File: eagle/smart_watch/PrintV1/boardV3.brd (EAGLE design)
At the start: 100 x 80 mm, 62 parts, among them U1 MCP73831, U2 TPS61200, U3 MAX1704X, U4 V_REG_LDOSMD, Y1 16MHz

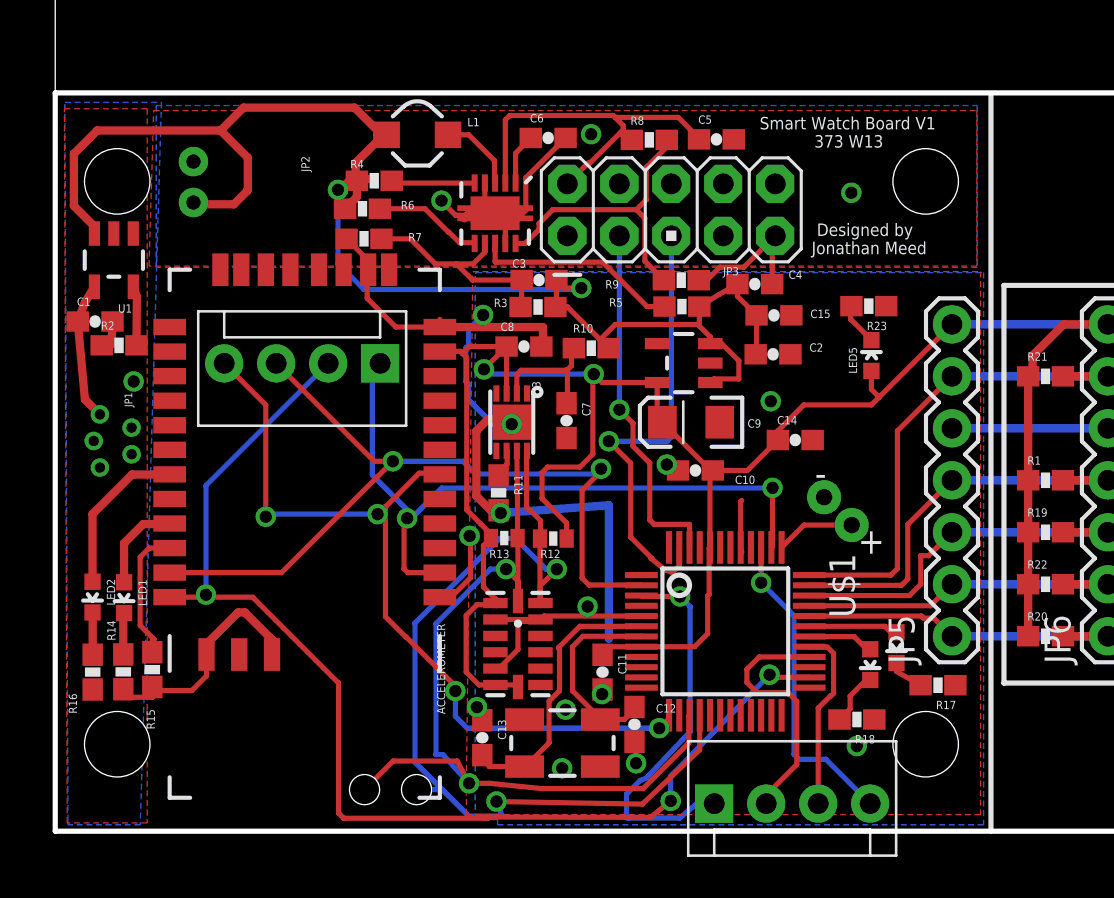
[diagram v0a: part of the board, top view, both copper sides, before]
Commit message: Fixed up git ignore for xpress;
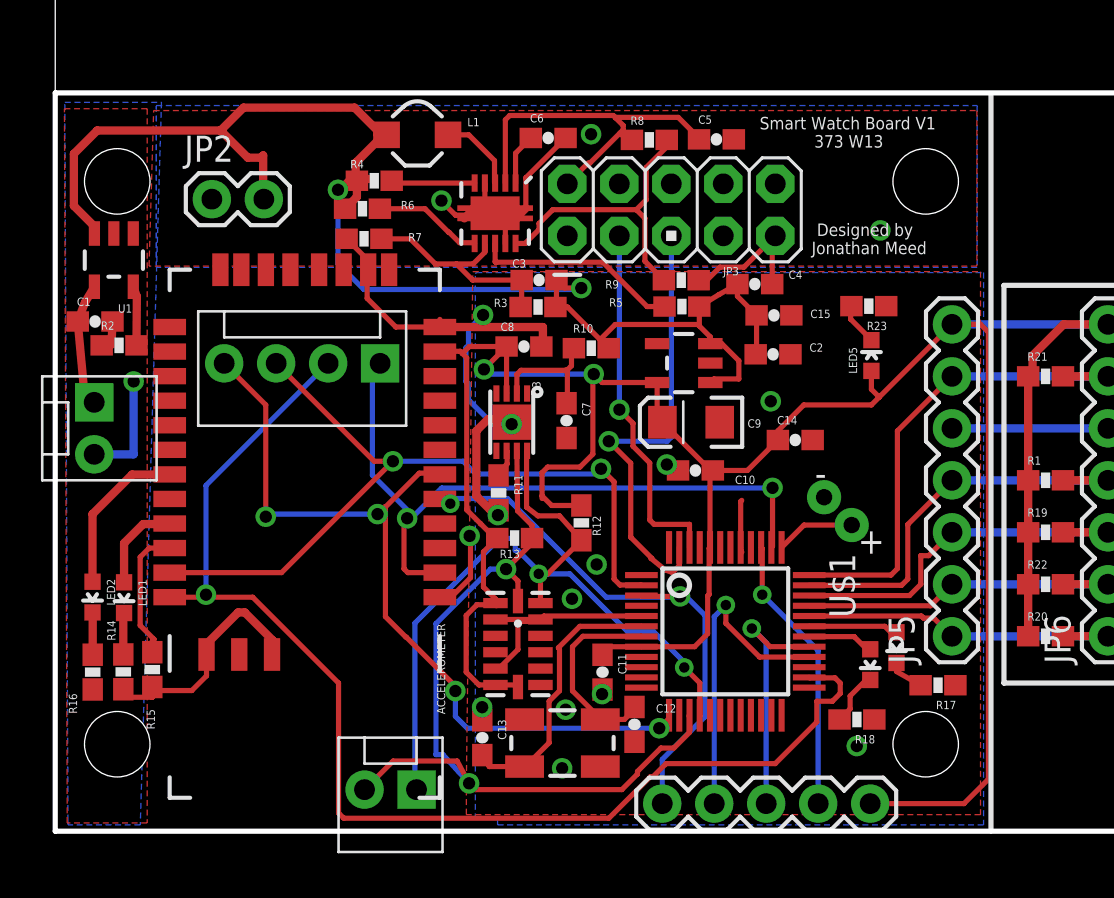
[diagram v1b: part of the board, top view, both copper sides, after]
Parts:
- removed JP1: USB_MICROB_PLUG-PTH, SparkFun-Connectors:MICRO-B-RA-TH
- added RECHARGE: (no value), SparkFun-Connectors:MOLEX-1X2
- I2C: device SparkFun-Connectors:1X02_PP_HOLES_ONLY -> SparkFun-Connectors:MOLEX-1X2
- JP2: device SparkFun-Connectors:JST-2-PTH-NS -> SparkFun-Connectors:1X02
- JP4: device SparkFun-Connectors:MOLEX-1X4 -> SparkFun-Connectors:1X05
- R12, R13: device SparkFun-Passives:0402-RES -> SparkFun-Resistors:0603-RES
- moved JP4 2.54 mm to (29.7, 1.35)
- moved R12 1.57 mm to (25.7, 15.1), turned to 90 degrees
- moved JP2 1.23 mm to (7.65, 30.9), turned to 0 degrees
- moved R13 0.51 mm to (22.4, 14.3)
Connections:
- net 3.3V: now also JP4.5
- net GND: now also RECHARGE.2; no longer JP1.5
- net VBUS: now also RECHARGE.1; no longer JP1.1
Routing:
- net 3.3V: track 108.8 -> 138.9 mm
- net JTAG_RESETX: track 18.8 -> 27.2 mm, vias 1 -> 2
- net SDA: track 45.9 -> 39.3 mm
- net GND: track 111.9 -> 105.5 mm
- net JTAG_TDO_SWOX: track 12.4 -> 15.6 mm, vias 0 -> 1
- net JTAG_TCLK_SWCLKX: track 9.00 -> 12.0 mm, vias 0 -> 1
- net MISO1: track 58.0 -> 60.2 mm, vias 3 -> 1
- net JTAG_TMS_SWDIOX: track 15.5 -> 13.7 mm
- net VBATT: track 74.0 -> 72.4 mm
- net SSEL1: track 40.1 -> 38.6 mm
- net SCL: track 41.7 -> 40.9 mm
- net VBUS: track 6.75 -> 6.23 mm
